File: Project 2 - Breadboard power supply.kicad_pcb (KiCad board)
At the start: 2 copper layers, 16 parts, among them J1 Conn_01x02_Pin, J2 Conn_01x02_Pin, J3 Conn_01x03_Pin, J4 Conn_01x03_Pin, J5 Screw_Terminal_01x02, J6 Barrel_Jack_Switch, J7 Screw_Terminal_01x02, U1 LM7805_TO220, U2 LM317_TO-220

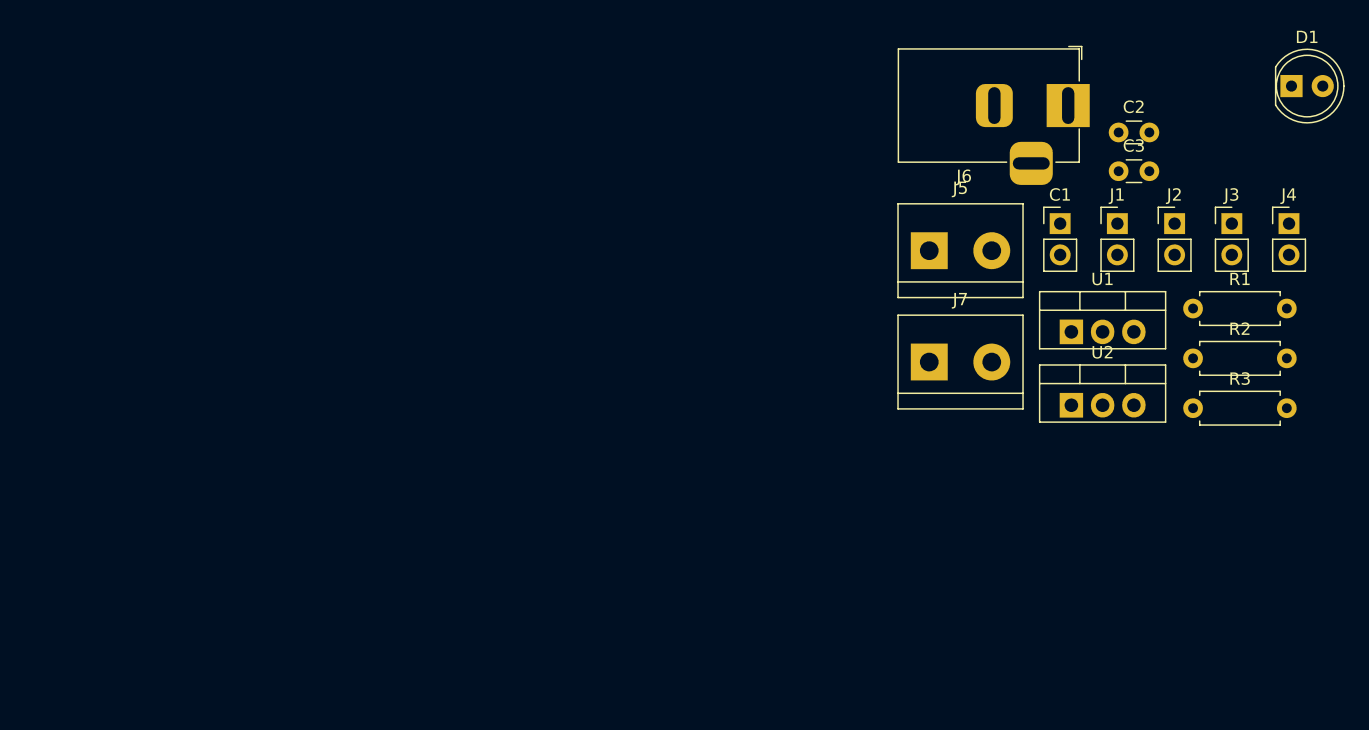
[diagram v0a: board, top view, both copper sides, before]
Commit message: update edges with arch
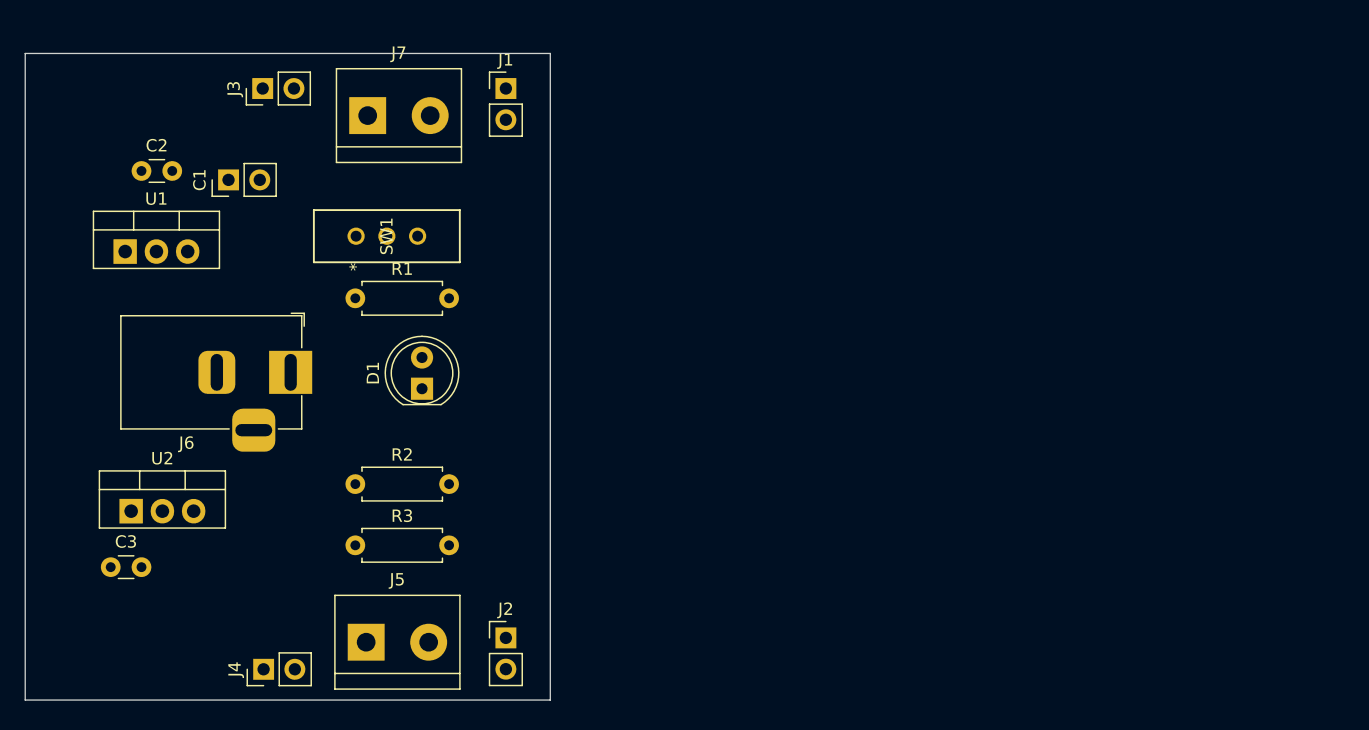
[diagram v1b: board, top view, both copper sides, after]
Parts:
- added SW1: EG1218, EG1218:SW_1218_EWI, F.Cu at (74.2, 67.3)
- moved J4 90.9 mm to (66.7, 102.5), turned to 90 degrees
- moved C3 88.0 mm to (54.3, 94.2)
- moved J3 79.5 mm to (66.6, 55.3), turned to 90 degrees
- moved C2 79.5 mm to (56.8, 62.0)
- moved U1 77.2 mm to (55.5, 68.5)
- moved U2 76.9 mm to (55.9, 89.7)
- moved D1 74.8 mm to (79.6, 79.7), turned to 90 degrees
- moved R3 69.0 mm to (74.2, 92.4)
- moved R2 68.8 mm to (74.2, 87.5)
- moved R1 68.1 mm to (74.2, 72.3)
- moved C1 67.7 mm to (63.9, 62.7), turned to 90 degrees
- moved J6 66.8 mm to (68.9, 78.4)
- moved J2 63.9 mm to (86.4, 100.0)
- moved J5 55.7 mm to (75.0, 100.3)
- moved J1 50.9 mm to (86.4, 55.3)
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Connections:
- C1 pad 1: unconnected-(C1-Pad1) -> /12V
- C1 pad 2: unconnected-(C1-Pad2) -> GND
- C2 pad 1: unconnected-(C2-Pad1) -> /5V
- C2 pad 2: unconnected-(C2-Pad2) -> GND
- C3 pad 1: unconnected-(C3-Pad1) -> /3.3V
- C3 pad 2: unconnected-(C3-Pad2) -> GND
- D1 pad 1: unconnected-(D1-K-Pad1) -> GND
- D1 pad 2: unconnected-(D1-A-Pad2) -> Net-(D1-A)
- J1 pad 1: unconnected-(J1-Pin_1-Pad1) -> GND
- J1 pad 2: unconnected-(J1-Pin_2-Pad2) -> /PWR_OUTPUT
- J2 pad 1: unconnected-(J2-Pin_1-Pad1) -> GND
- J2 pad 2: unconnected-(J2-Pin_2-Pad2) -> /PWR_OUTPUT
- J3 pad 1: unconnected-(J3-Pin_1-Pad1) -> /3.3V
- J3 pad 2: unconnected-(J3-Pin_2-Pad2) -> /PWR_OUTPUT
- J4 pad 1: unconnected-(J4-Pin_1-Pad1) -> /3.3V
- J4 pad 2: unconnected-(J4-Pin_2-Pad2) -> /PWR_OUTPUT
- J5 pad 1: unconnected-(J5-Pin_1-Pad1) -> GND
- J5 pad 2: unconnected-(J5-Pin_2-Pad2) -> /PWR_OUTPUT
- J6 pad 1: unconnected-(J6-Pad1) -> /PWR_INPUT
- J6 pad 2: unconnected-(J6-Pad2) -> GND
- J6 pad 3: unconnected-(J6-Pad3) -> GND
- J7 pad 1: unconnected-(J7-Pin_1-Pad1) -> GND
- J7 pad 2: unconnected-(J7-Pin_2-Pad2) -> /PWR_OUTPUT
- R1 pad 1: unconnected-(R1-Pad1) -> Net-(U2-ADJ)
- R1 pad 2: unconnected-(R1-Pad2) -> /3.3V
- R2 pad 1: unconnected-(R2-Pad1) -> Net-(D1-A)
- R2 pad 2: unconnected-(R2-Pad2) -> /12V
- R3 pad 1: unconnected-(R3-Pad1) -> GND
- R3 pad 2: unconnected-(R3-Pad2) -> Net-(U2-ADJ)
- U1 pad 1: unconnected-(U1-VI-Pad1) -> /12V
- U1 pad 2: unconnected-(U1-GND-Pad2) -> GND
- U1 pad 3: unconnected-(U1-VO-Pad3) -> /5V
- U2 pad 1: unconnected-(U2-ADJ-Pad1) -> Net-(U2-ADJ)
- U2 pad 2: unconnected-(U2-VO-Pad2) -> /3.3V
- U2 pad 3: unconnected-(U2-VI-Pad3) -> /12V
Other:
- board outline added: 42.7 x 52.5 mm

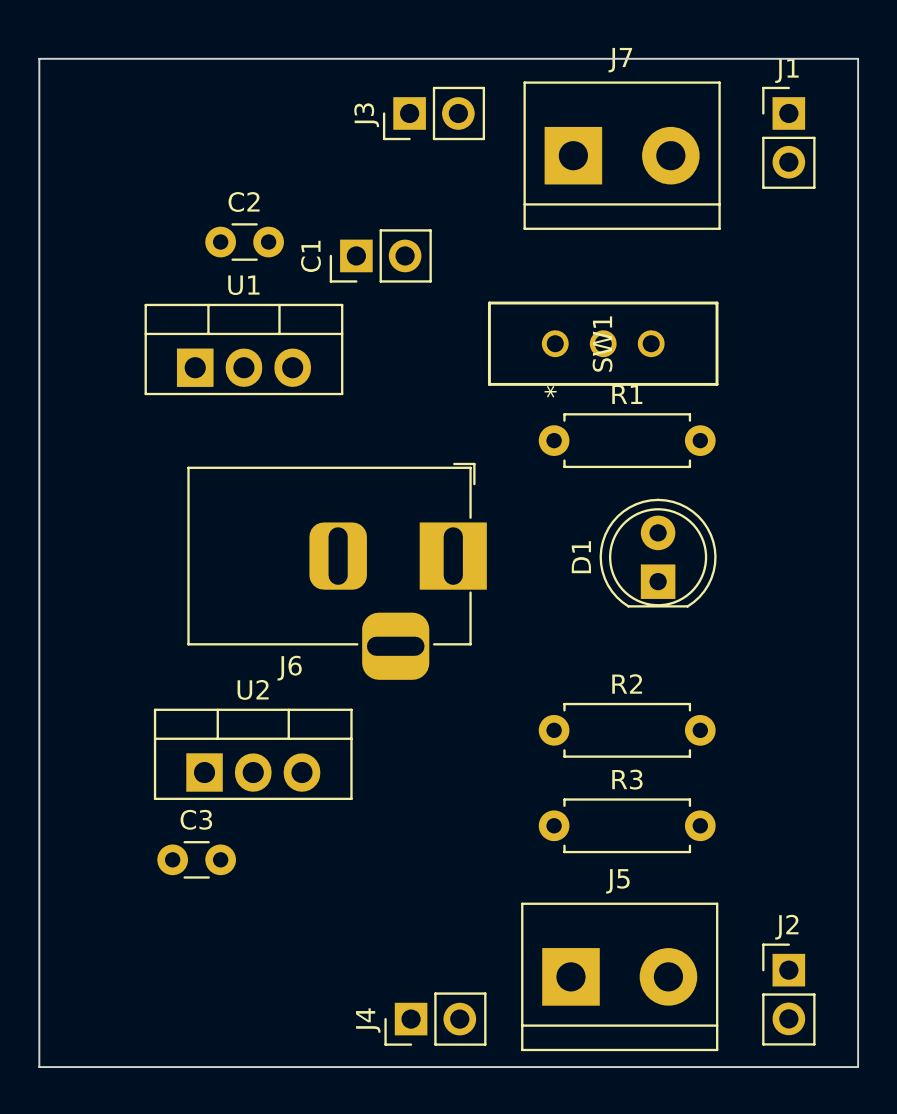
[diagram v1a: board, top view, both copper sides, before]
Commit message: added routing and silkscreen
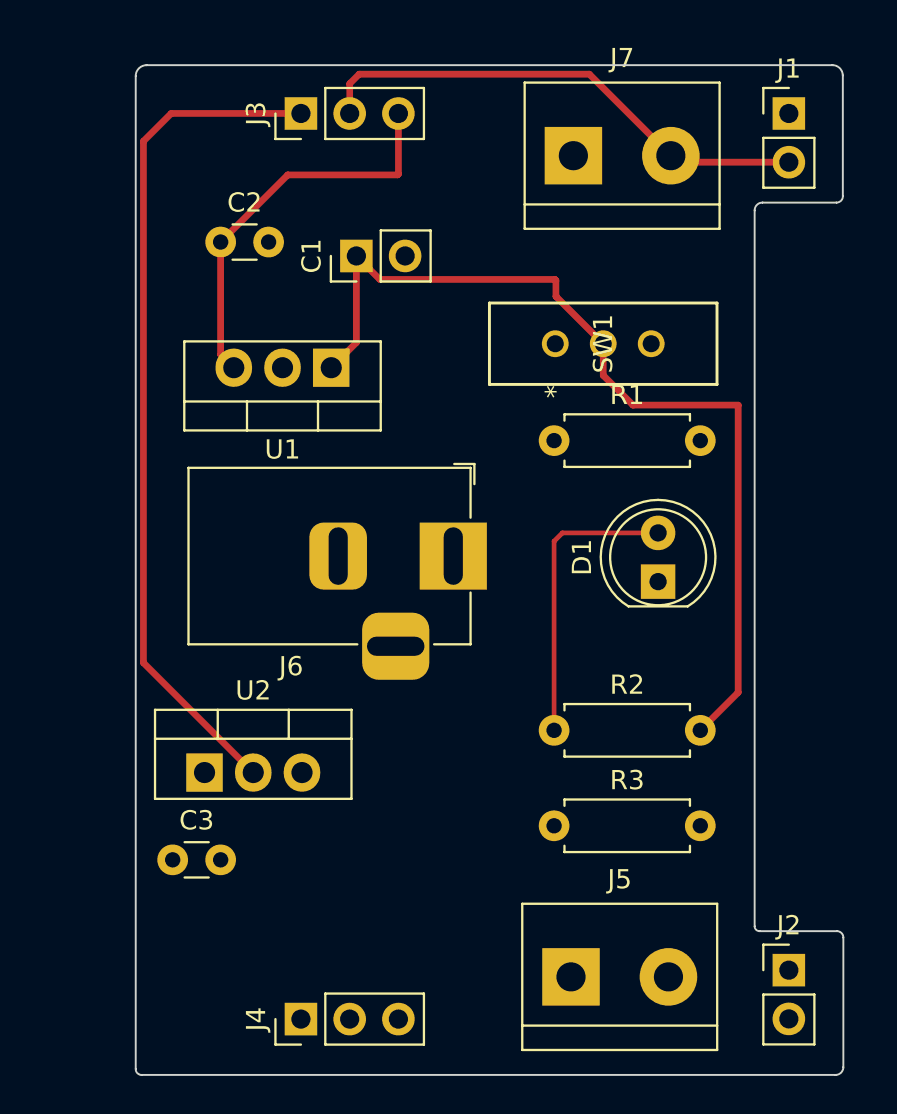
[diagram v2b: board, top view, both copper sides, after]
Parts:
- J3, J4: footprint Connector_PinHeader_2.54mm:PinHeader_1x02_P2.54mm_Vertical -> Connector_PinHeader_2.54mm:PinHeader_1x03_P2.54mm_Vertical
- moved U1 7.09 mm to (62.5, 68.5), turned to 180 degrees
- moved J4 5.74 mm to (61.0, 102.5)
- moved J3 5.66 mm to (61.0, 55.3)
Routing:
- net /12V: track 0.00 -> 48.7 mm
- net /3.3V: track 0.00 -> 44.1 mm
- net /PWR_OUTPUT: track 0.00 -> 26.5 mm
- net /5V: track 0.00 -> 20.7 mm
- net Net-(D1-A): track 0.00 -> 15.5 mm
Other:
- board size 42.7 x 52.5 mm -> 36.9 x 52.6 mm

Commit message: make measurements
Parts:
- added REF**: KiCad-Logo2_5mm_SilkScreen, Symbol:KiCad-Logo2_5mm_SilkScreen, B.Cu at (60.9, 79.3)
- moved U2 5.88 mm to (61.5, 87.8), turned to 180 degrees
- moved U1 0.46 mm to (63.0, 68.5)
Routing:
- net /PWR_OUTPUT: track 26.5 -> 98.5 mm
- net /5V: track 20.7 -> 68.8 mm
- net Net-(U2-ADJ): track 0.00 -> 46.7 mm
- net /3.3V: track 44.1 -> 83.4 mm
- net /12V: track 48.7 -> 76.5 mm
- net /PWR_INPUT: track 0.00 -> 13.3 mm
- added copper zone on B.Cu, net GND
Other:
- board text added: "+"
- board text added: "-"
- board text added: "3.3V"
- board text added: "5V"
- board text added: "GND"
- board text added: "OFF"
- board text added: "ON"
- board text added: "v1.0"
